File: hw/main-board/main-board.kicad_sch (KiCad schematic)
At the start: 68 parts, among them J1 USB_C_Receptacle_USB2.0_16P, J2 S4B-XH-A_LF__SN_, J3 S4B-XH-A_LF__SN_, J4 Conn_ARM_JTAG_SWD_10, Q1 AONR21307, U1 HUSB238_xxxDD, U2 AP63205WU, U3 AP2112K-3.3, U4 PTR54L, U5 TMC2226-SA, U6 TMC2226-SA, U7 KTD2026BEWE-TR

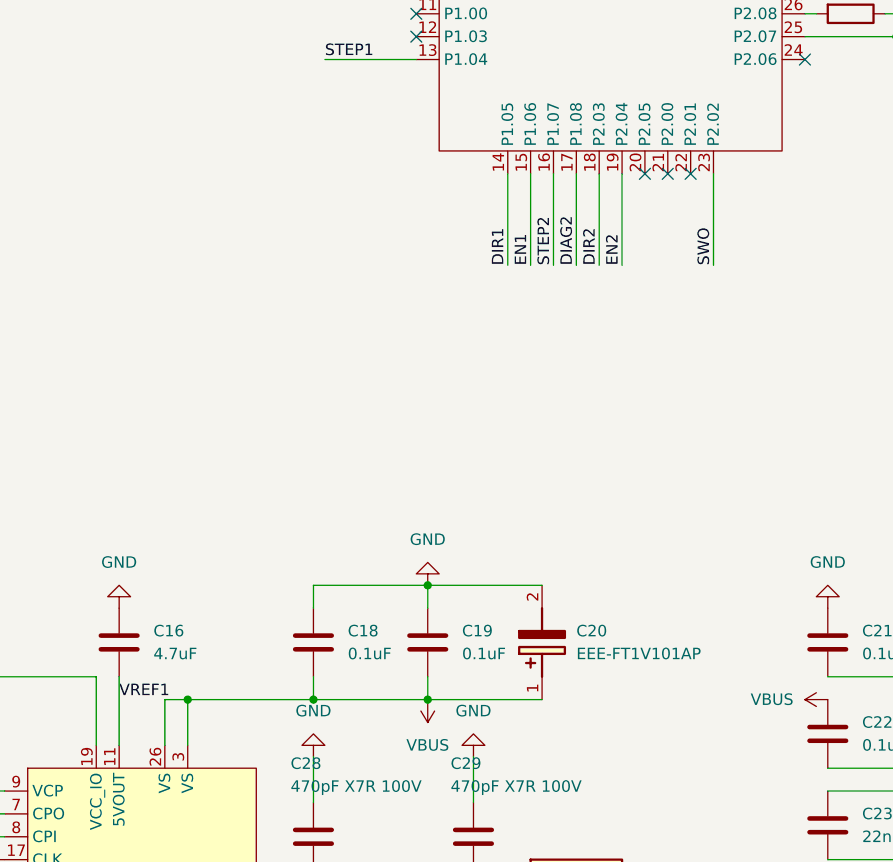
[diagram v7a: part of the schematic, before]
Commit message: Add component classes for TMC2226 circuit
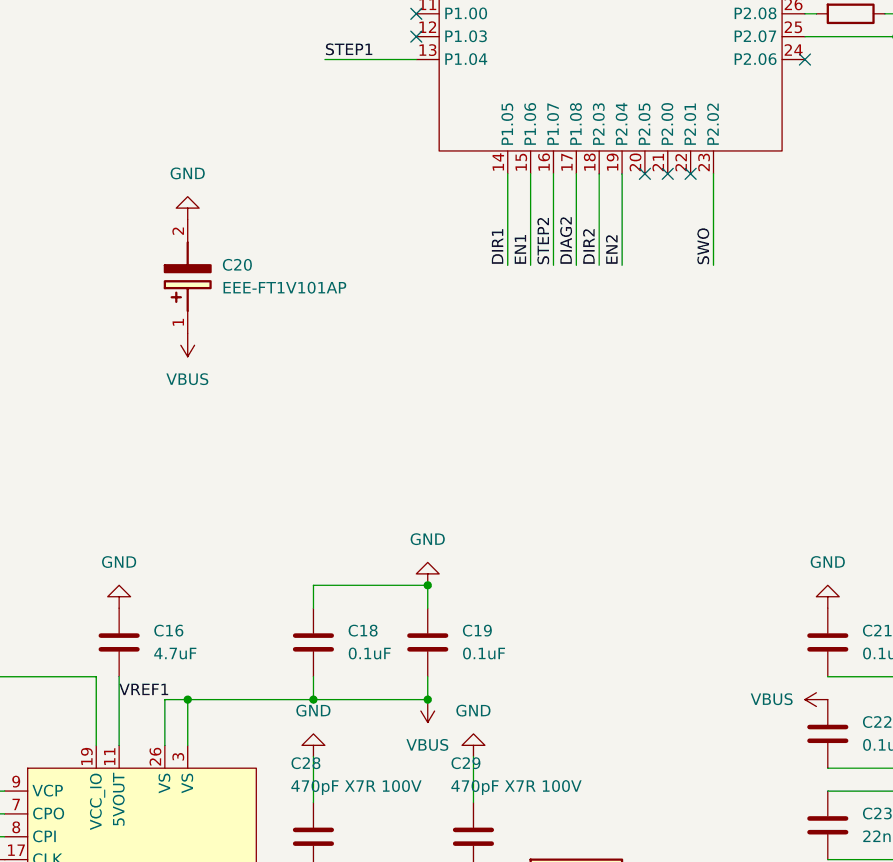
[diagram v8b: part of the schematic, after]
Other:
- moved on the sheet: C20
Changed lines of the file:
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@@
 	(wire
 		(pts
-			(xy 245.11 160.02) (xy 257.81 160.02)
-		)
-		(stroke
-			(width 0)
-			(type default)
-		)
-	)
-	(wire
-		(pts
 			(xy 81.28 234.95) (xy 77.47 234.95)
 		)
@@
 	(wire
 		(pts
-			(xy 245.11 147.32) (xy 257.81 147.32)
-		)
-		(stroke
-			(width 0)
-			(type default)
-		)
-	)
-	(wire
-		(pts
 			(xy 266.7 101.6) (xy 266.7 111.76)
 		)
@@
 			(justify left bottom)
 		)
-		(property "Netclass" "Default"
+		(property "Netclass" "DRV2"
 			(at 402.0185 135.89 0)
 			(hide yes)
@@
 			(justify left bottom)
 		)
-		(property "Netclass" "Default"
+		(property "Netclass" "DRV1"
 			(at 278.8285 135.89 0)
 			(hide yes)
@@
 		)
 		(property "Component Class" "DRV1"
-			(at 278.13 133.858 0)
+			(at 278.892 133.858 0)
 			(show_name no)
 			(do_not_autoplace no)
@@
 	)
 	(symbol
+		(lib_id "power:GND")
+		(at 218.44 106.68 180)
+		(unit 1)
+		(body_style 1)
+		(exclude_from_sim no)
+		(in_bom yes)
+		(on_board yes)
+		(in_pos_files yes)
+		(dnp no)
+		(fields_autoplaced yes)
+		(property "Reference" "#PWR061"
+			(at 218.44 100.33 0)
+			(hide yes)
+			(show_name no)
+			(do_not_autoplace no)
+			(effects
+				(font
+					(size 1.27 1.27)
+				)
+			)
+		)
+		(property "Value" "GND"
+			(at 218.44 101.6 0)
+			(show_name no)
+			(do_not_autoplace no)
+			(effects
+				(font
+					(size 1.27 1.27)
+				)
+			)
+		)
+		(property "Footprint" ""
+			(at 218.44 106.68 0)
+			(hide yes)
+			(show_name no)
+			(do_not_autoplace no)
+			(effects
+				(font
+					(size 1.27 1.27)
+				)
+			)
+		)
+		(property "Datasheet" ""
+			(at 218.44 106.68 0)
+			(hide yes)
+			(show_name no)
+			(do_not_autoplace no)
+			(effects
+				(font
+					(size 1.27 1.27)
+				)
+			)
+		)
+		(property "Description" "Power symbol creates a global label with name \"GND\" , ground"
+			(at 218.44 106.68 0)
+			(hide yes)
+			(show_name no)
+			(do_not_autoplace no)
+			(effects
+				(font
+					(size 1.27 1.27)
+				)
+			)
+		)
+		(pin "1"
+		)
+		(instances
+			(project "main-board"
+				(path "/fe215afa-a228-4dbb-8560-a0753323a3f2"
+					(reference "#PWR061")
+					(unit 1)
+				)
+			)
+		)
+	)
+	(symbol
 		(lib_id "Samacsys:EEE-FT1V101AP")
-		(at 257.81 160.02 90)
+		(at 218.44 119.38 90)
 		(unit 1)
 		(body_style 1)
@@
 		(fields_autoplaced yes)
 		(property "Reference" "C20"
-			(at 261.62 152.3999 90)
+			(at 222.25 111.7599 90)
 			(show_name no)
 			(do_not_autoplace no)
@@
 		)
 		(property "Value" "EEE-FT1V101AP"
-			(at 261.62 154.9399 90)
+			(at 222.25 114.2999 90)
 			(show_name no)
 			(do_not_autoplace no)
@@
 		)
 		(property "Footprint" "EEE1AA101SP"
-			(at 354 151.13 0)
+			(at 314.63 110.49 0)
 			(hide yes)
 			(show_name no)
@@
 		)
 		(property "Datasheet" "http://industrial.panasonic.com/cdbs/www-data/pdf/RDE0000/ABA0000C1240.pdf"
-			(at 454 151.13 0)
+			(at 414.63 110.49 0)
 			(hide yes)
 			(show_name no)
@@
 		)
 		(property "Description" "Aluminum Electrolytic Capacitors - SMD 100uF 35volts 6.3x5.8mm SMD"
-			(at 257.81 160.02 0)
+			(at 218.44 119.38 0)
 			(hide yes)
 			(show_name no)
@@
 		)
 		(property "Height" "7.8"
-			(at 654 151.13 0)
+			(at 614.63 110.49 0)
 			(hide yes)
 			(show_name no)
@@
 		)
 		(property "Manufacturer_Name" "Panasonic"
-			(at 754 151.13 0)
+			(at 714.63 110.49 0)
 			(hide yes)
 			(show_name no)
@@
 		)
 		(property "Manufacturer_Part_Number" "EEE-FT1V101AP"
-			(at 854 151.13 0)
+			(at 814.63 110.49 0)
 			(hide yes)
 			(show_name no)
@@
 		)
 		(property "Mouser Part Number" "667-EEE-FT1V101AP"
-			(at 954 151.13 0)
+			(at 914.63 110.49 0)
 			(hide yes)
 			(show_name no)
@@
 		)
 		(property "Mouser Price/Stock" "https://www.mouser.co.uk/ProductDetail/Panasonic/EEE-FT1V101AP?qs=CMJjuEs1%252BuEsbOqam%2FkTqg%3D%3D"
-			(at 1054 151.13 0)
+			(at 1014.63 110.49 0)
 			(hide yes)
 			(show_name no)
@@
 		)
 		(property "Arrow Part Number" "EEE-FT1V101AP"
-			(at 1154 151.13 0)
+			(at 1114.63 110.49 0)
 			(hide yes)
 			(show_name no)
@@
 		)
 		(property "Arrow Price/Stock" "https://www.arrow.com/en/products/eeeft1v101ap/panasonic.html?utm_currency=USD&region=nac"
-			(at 1254 151.13 0)
+			(at 1214.63 110.49 0)
 			(hide yes)
 			(show_name no)
@@
 					(unit 1)
 				)
+			)
+		)
+	)
+	(symbol
+		(lib_id "power:VBUS")
+		(at 218.44 119.38 180)
+		(unit 1)
+		(body_style 1)
+		(exclude_from_sim no)
+		(in_bom yes)
+		(on_board yes)
+		(in_pos_files yes)
+		(dnp no)
+		(fields_autoplaced yes)
+		(property "Reference" "#PWR060"
+			(at 218.44 115.57 0)
+			(hide yes)
+			(show_name no)
+			(do_not_autoplace no)
+			(effects
+				(font
+					(size 1.27 1.27)
+				)
+			)
+		)
+		(property "Value" "VBUS"
+			(at 218.44 124.46 0)
+			(show_name no)
+			(do_not_autoplace no)
+			(effects
+				(font
+					(size 1.27 1.27)
+				)
+			)
+		)
+		(property "Footprint" ""
+			(at 218.44 119.38 0)
+			(hide yes)
+			(show_name no)
+			(do_not_autoplace no)
+			(effects
+				(font
+					(size 1.27 1.27)
+				)
+			)
+		)
+		(property "Datasheet" ""
+			(at 218.44 119.38 0)
+			(hide yes)
+			(show_name no)
+			(do_not_autoplace no)
+			(effects
+				(font
+					(size 1.27 1.27)
+				)
+			)
+		)
+		(property "Description" "Power symbol creates a global label with name \"VBUS\""
+			(at 218.44 119.38 0)
+			(hide yes)
+			(show_name no)
+			(do_not_autoplace no)
+			(effects
+				(font
+					(size 1.27 1.27)
+				)
+			)
+		)
+		(pin "1"
+		)
+		(instances
+			(project "main-board"
+				(path "/fe215afa-a228-4dbb-8560-a0753323a3f2"
+					(reference "#PWR060")
+					(unit 1)
+				)
